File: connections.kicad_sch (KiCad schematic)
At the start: 3 parts, among them J1 USB_B

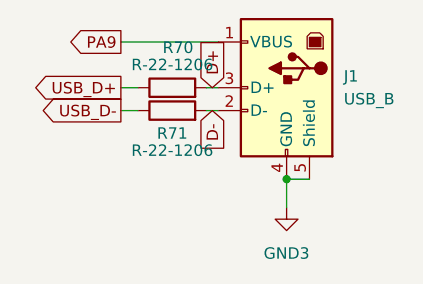
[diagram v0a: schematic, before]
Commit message: Changed all R to 0603
all res to 0603 and changed JACK to LED Jack (for fancy)
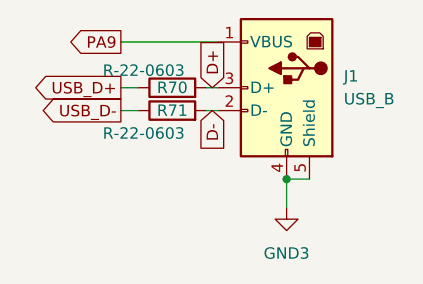
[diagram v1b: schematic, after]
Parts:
- R70, R71: value R-22-1206 -> R-22-0603; footprint Resistor_SMD:R_1206_3216Metric_Pad1.30x1.75mm_HandSolder -> Resistor_SMD:R_0201_0603Metric_Pad0.64x0.40mm_HandSolder; symbol eurorack:R-22-1206 -> eurorack:R-22-0603; P 1/4W -> 0.1
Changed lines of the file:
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@@
     )
   )
-  (symbol (lib_id "eurorack:R-22-1206") (at 31.75 31.115 90) (unit 1)
+  (symbol (lib_id "eurorack:R-22-0603") (at 31.75 31.115 90) (unit 1)
     (in_bom yes) (on_board yes) (dnp no)
-    (property "Reference" "R71" (at 31.75 33.655 90)
+    (property "Reference" "R71" (at 31.75 31.115 90)
       (effects (font (size 1.27 1.27)))
     )
-    (property "Value" "R-22-1206" (at 31.75 35.56 90)
+    (property "Value" "R-22-0603" (at 28.575 33.655 90)
       (effects (font (size 1.27 1.27)))
     )
-    (property "Footprint" "Resistor_SMD:R_1206_3216Metric_Pad1.30x1.75mm_HandSolder" (at 31.75 32.893 90)
+    (property "Footprint" "Resistor_SMD:R_0201_0603Metric_Pad0.64x0.40mm_HandSolder" (at 31.75 32.893 90)
       (effects (font (size 1.27 1.27)) hide)
     )
@@
       (effects (font (size 1.27 1.27)) hide)
     )
-    (property "P" "1/4W" (at 31.75 27.305 90)
+    (property "P" "0.1" (at 31.75 31.115 0)
       (effects (font (size 1.27 1.27)) hide)
     )
@@
     )
   )
-  (symbol (lib_id "eurorack:R-22-1206") (at 31.75 28.575 90) (unit 1)
+  (symbol (lib_id "eurorack:R-22-0603") (at 31.75 28.575 90) (unit 1)
     (in_bom yes) (on_board yes) (dnp no)
-    (property "Reference" "R70" (at 32.385 24.13 90)
+    (property "Reference" "R70" (at 31.75 28.575 90)
       (effects (font (size 1.27 1.27)))
     )
-    (property "Value" "R-22-1206" (at 31.75 26.035 90)
+    (property "Value" "R-22-0603" (at 28.575 26.67 90)
       (effects (font (size 1.27 1.27)))
     )
-    (property "Footprint" "Resistor_SMD:R_1206_3216Metric_Pad1.30x1.75mm_HandSolder" (at 31.75 30.353 90)
+    (property "Footprint" "Resistor_SMD:R_0201_0603Metric_Pad0.64x0.40mm_HandSolder" (at 31.75 30.353 90)
       (effects (font (size 1.27 1.27)) hide)
     )
@@
       (effects (font (size 1.27 1.27)) hide)
     )
-    (property "P" "1/4W" (at 31.75 24.765 90)
+    (property "P" "0.1" (at 31.75 28.575 0)
       (effects (font (size 1.27 1.27)) hide)
     )
